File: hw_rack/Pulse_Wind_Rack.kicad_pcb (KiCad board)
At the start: 2 copper layers, 12 parts, among them J1 PH2.00, J2 PH2.00, J3 AudioJack4, U1 ME6206A33XG

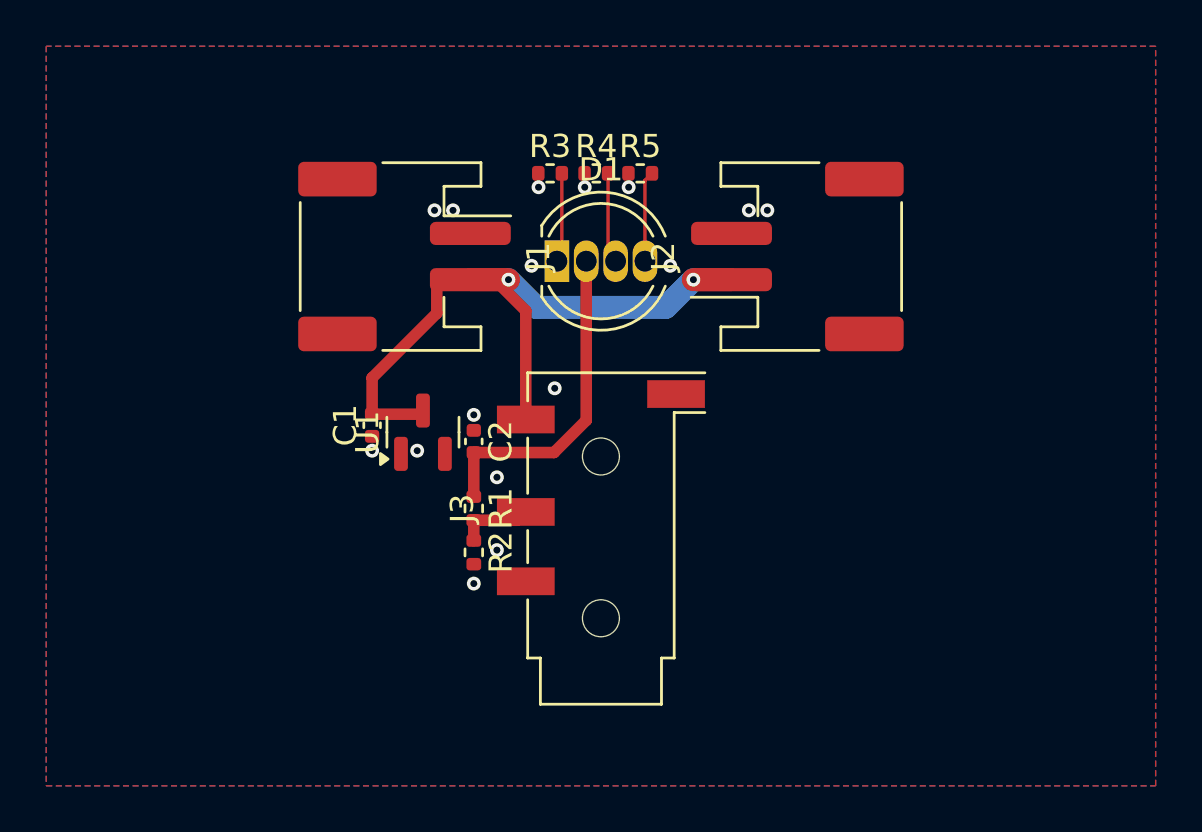
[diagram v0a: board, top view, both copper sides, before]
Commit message: fw: Revise rack board layout & routing
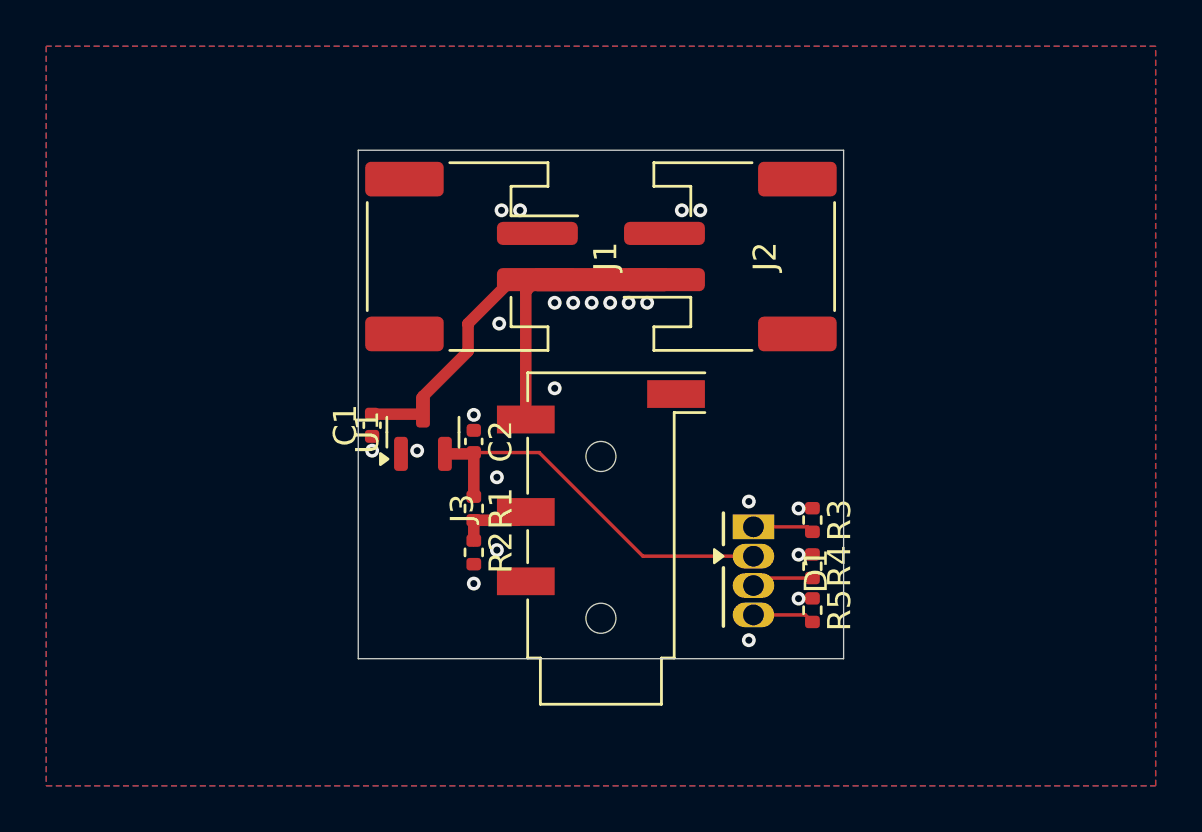
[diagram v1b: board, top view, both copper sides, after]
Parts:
- moved R5 20.3 mm to (159.2, 104.4), turned to -90 degrees
- moved R4 19.4 mm to (159.2, 102.5), turned to -90 degrees
- moved R3 18.8 mm to (159.2, 100.5), turned to -90 degrees
- moved D1 14.3 mm to (156.6, 100.8), turned to -90 degrees
- moved J1 2.90 mm to (144.4, 89.1)
- moved J2 2.90 mm to (155.6, 89.1)
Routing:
- net V+: track 30.6 -> 22.4 mm, vias 2 -> 0
- net +3V3: track 14.2 -> 17.1 mm
- net Net-(D1-BK): track 3.93 -> 2.68 mm
- net Net-(D1-GK): track 3.93 -> 2.68 mm
- net Net-(D1-RK): track 3.89 -> 2.64 mm
- net GND: vias 16 -> 23
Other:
- board outline added: 21 x 22 mm

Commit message: hw: Finalize rack board design
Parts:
- added G***: LOGO, LOGO, B.Cu at (152.8, 87.3)
- added G***: LOGO, LOGO, B.Cu at (157.8, 87.1)
- moved R3 0.30 mm to (159.4, 100.5)
- moved R4 0.30 mm to (159.4, 102.5)
- moved R5 0.30 mm to (159.4, 104.4)
- moved D1 0.20 mm to (156.4, 100.8)
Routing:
- net GND: vias 23 -> 25
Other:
- outline, holes or cut-outs redrawn
- board text added: "+"
- board text added: "<25-"
- board text added: ">"
- board text added: "Rev. 1"
- board text added: "大暑"

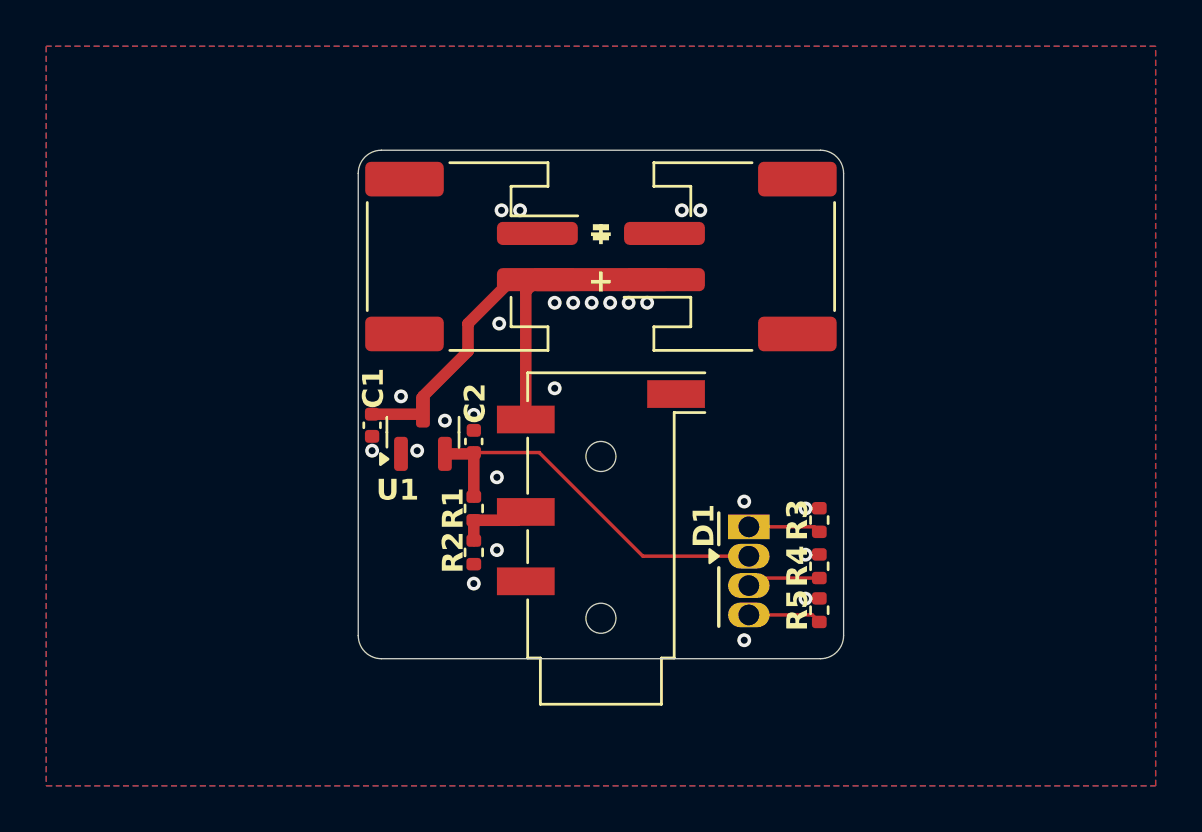
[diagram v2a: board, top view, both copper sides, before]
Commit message: hw: Add polyfuse in rack board
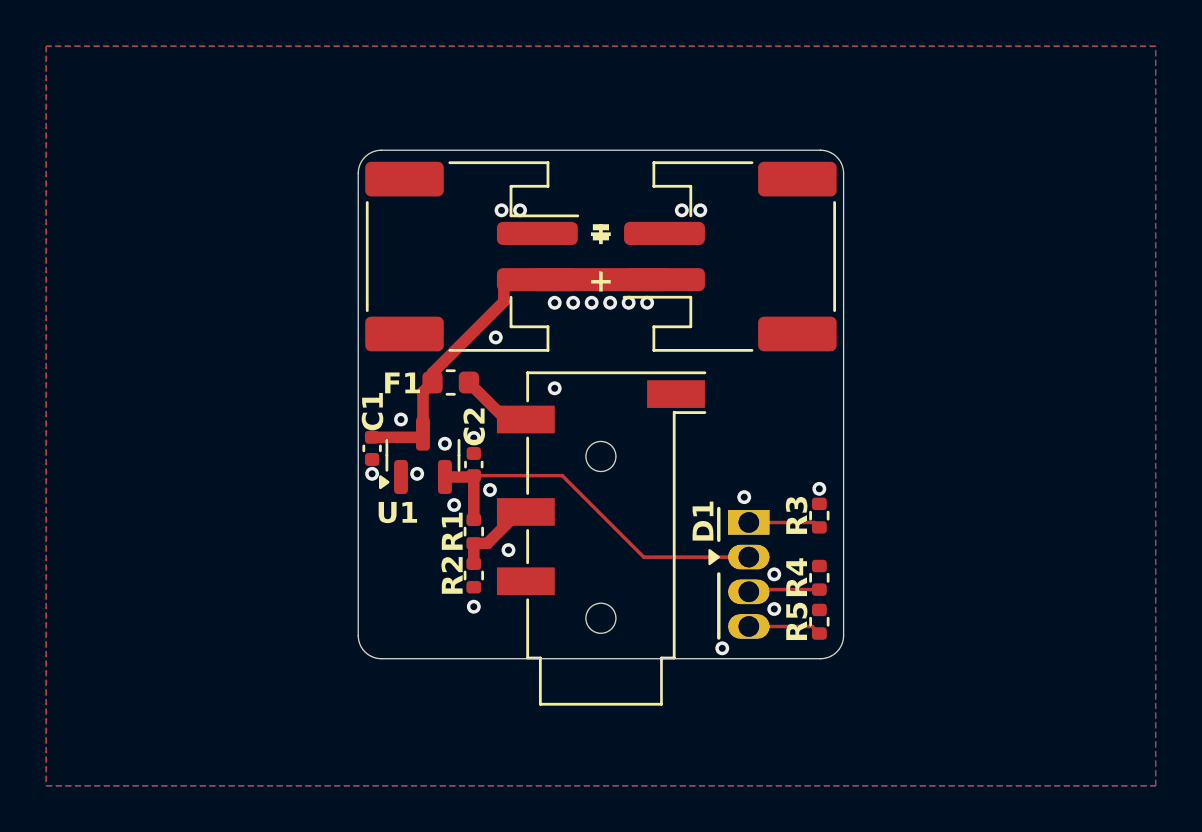
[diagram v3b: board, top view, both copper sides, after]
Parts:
- added F1: 0.2A, Fuse:Fuse_0603_1608Metric, F.Cu at (143.5, 94.5)
- moved C1 1.00 mm to (140.1, 97.4)
- moved C2 1.00 mm to (144.5, 98.1)
- moved R1 1.00 mm to (144.5, 101.0)
- moved R2 1.00 mm to (144.5, 102.9)
- moved U1 1.00 mm to (142.3, 97.7)
- moved R4 0.50 mm to (159.4, 103.0)
- moved R5 0.50 mm to (159.4, 104.9)
- moved D1 0.19 mm to (156.4, 100.6)
- moved R3 0.19 mm to (159.4, 100.3)
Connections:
- J3 pad T: V+ -> Net-(F1-Pad1)
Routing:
- net V+: track 22.4 -> 17.3 mm
- net Net-(F1-Pad1): track 0.00 -> 3.13 mm
- net +3V3: track 17.1 -> 16.5 mm
- net GND: vias 25 -> 26
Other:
- board text added: "Rev. 2"
- board text added: "ayu.land/pulse?id=K2_??"
- board text added: "立秋"
- board text removed: "Rev. 1"
- board text removed: "大暑"
